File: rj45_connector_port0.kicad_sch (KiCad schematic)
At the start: 4 parts, among them J1 1840888-1

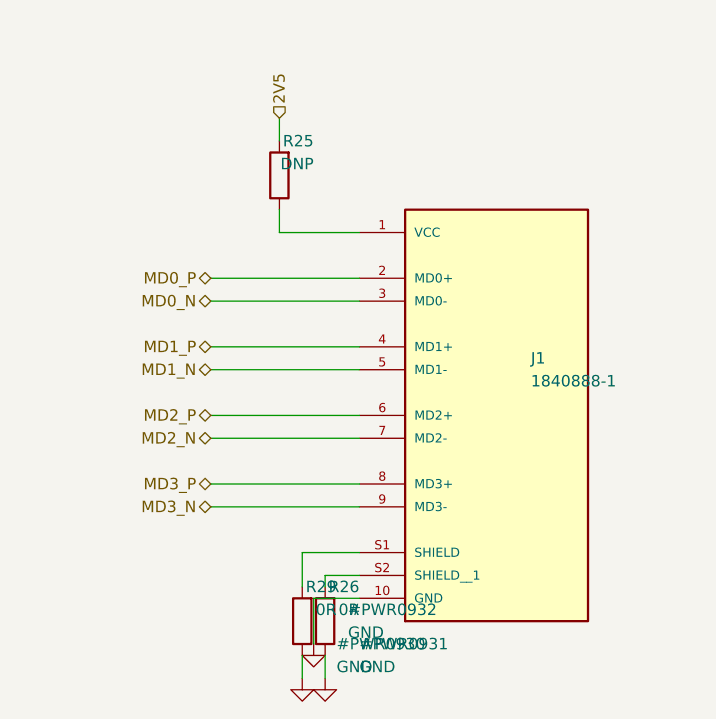
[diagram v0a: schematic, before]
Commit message: Migrate RJ45 port sheet to KL library symbols
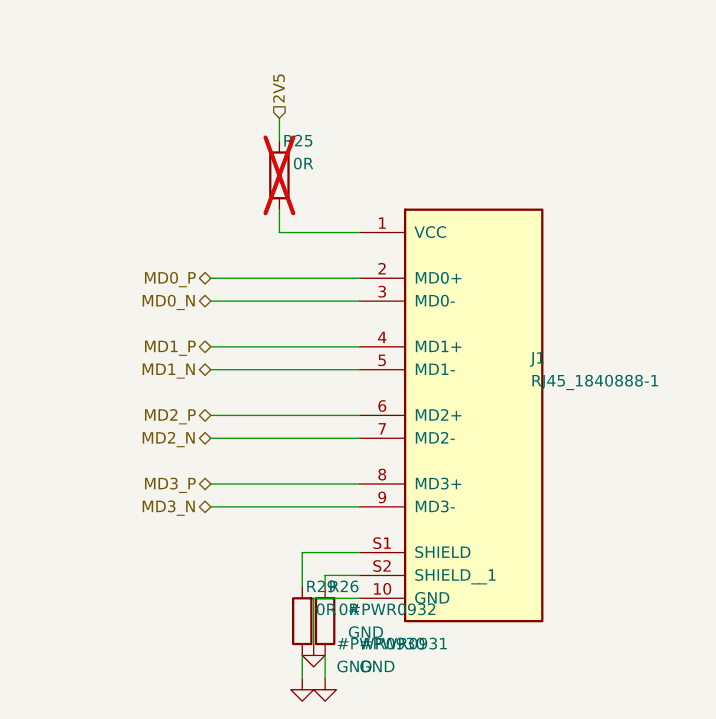
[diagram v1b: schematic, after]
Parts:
- J1: value 1840888-1 -> RJ45_1840888-1; footprint 1840888_1:BEL_1840888-1 -> KL_Footprints:BEL_1840888-1; symbol 1840888-1:1840888-1 -> KL_Conn_Data:RJ45_1840888-1; Digikey (none) -> TBD; LCSC (none) -> TBD; MPN (none) -> 1840888-1; Mouser (none) -> TBD
- R25: value DNP -> 0R; footprint Resistor_SMD:R_0402_1005Metric_Pad0.72x0.64mm_HandSolder -> KL_Footprints:R_0402; symbol Device:R -> KL_R:R_0R_0.063W_5pct_0402; Digikey (none) -> TBD; LCSC (none) -> TBD; MPN (none) -> CRCW04020000Z0EDC; Mouser (none) -> 71-CRCW04020000Z0EDC; Package_in_inch (none) -> 0402; Power_in_W (none) -> 0.063; Tolerance_in_pct (none) -> 5; now not fitted
- R26, R29: footprint Resistor_SMD:R_0402_1005Metric_Pad0.72x0.64mm_HandSolder -> KL_Footprints:R_0402; symbol Device:R -> KL_R:R_0R_0.063W_5pct_0402; Digikey (none) -> TBD; LCSC (none) -> TBD; MPN (none) -> CRCW04020000Z0EDC; Mouser (none) -> 71-CRCW04020000Z0EDC; Package_in_inch (none) -> 0402; Power_in_W (none) -> 0.063; Tolerance_in_pct (none) -> 5
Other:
- moved on the sheet: J1

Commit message: Apply signal naming convention to all nets
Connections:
- net 2V5 renamed VDD_2V5
- net MD0_N renamed MDI0_PHY_RJ45_N
- net MD0_P renamed MDI0_PHY_RJ45_P
- net MD1_N renamed MDI1_PHY_RJ45_N
- net MD1_P renamed MDI1_PHY_RJ45_P
- net MD2_N renamed MDI2_PHY_RJ45_N
- net MD2_P renamed MDI2_PHY_RJ45_P
- net MD3_N renamed MDI3_PHY_RJ45_N
- net MD3_P renamed MDI3_PHY_RJ45_P
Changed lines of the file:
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@@
 		)
 	)
-	(hierarchical_label "MD0_P"
+	(hierarchical_label "MDI0_PHY_RJ45_P"
 		(shape bidirectional)
 		(at 133.35 63.5 180)
@@
 		)
 	)
-	(hierarchical_label "MD0_N"
+	(hierarchical_label "MDI0_PHY_RJ45_N"
 		(shape bidirectional)
 		(at 133.35 66.04 180)
@@
 		)
 	)
-	(hierarchical_label "MD1_P"
+	(hierarchical_label "MDI1_PHY_RJ45_P"
 		(shape bidirectional)
 		(at 133.35 71.12 180)
@@
 		)
 	)
-	(hierarchical_label "MD1_N"
+	(hierarchical_label "MDI1_PHY_RJ45_N"
 		(shape bidirectional)
 		(at 133.35 73.66 180)
@@
 		)
 	)
-	(hierarchical_label "MD2_P"
+	(hierarchical_label "MDI2_PHY_RJ45_P"
 		(shape bidirectional)
 		(at 133.35 78.74 180)
@@
 		)
 	)
-	(hierarchical_label "MD2_N"
+	(hierarchical_label "MDI2_PHY_RJ45_N"
 		(shape bidirectional)
 		(at 133.35 81.28 180)
@@
 		)
 	)
-	(hierarchical_label "MD3_P"
+	(hierarchical_label "MDI3_PHY_RJ45_P"
 		(shape bidirectional)
 		(at 133.35 86.36 180)
@@
 		)
 	)
-	(hierarchical_label "MD3_N"
+	(hierarchical_label "MDI3_PHY_RJ45_N"
 		(shape bidirectional)
 		(at 133.35 88.9 180)
@@
 		)
 	)
-	(hierarchical_label "2V5"
+	(hierarchical_label "VDD_2V5"
 		(shape input)
 		(at 140.97 45.72 90)
